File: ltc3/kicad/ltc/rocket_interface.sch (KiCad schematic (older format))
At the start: 68 parts, among them IC601 TLP3542, J601 RJ45, K601 RELAY_1C, K602 RELAY_1C, M601 W28-XQ1A-10, P601 BATT-IN, P602 CONN_01x02, P603 UMBILICAL, P604 43025-0200, P605 43045-0200, P606 S4B-PH-K, P607 43045-0200, P608 43025-0200, P609 PHR-4, Q601 PMV45EN, Q602 PMV45EN, Q603 ZVN4525E6, Q604 ZVN4525E6, Q605 ZVN4525E6, SW601 SPST, U601 CD74HC14, U602 SN65220DBV, U603 741G08

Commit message: LTC3: Split single-board design into two boards.
Separated the charge controller and cell protection circuitry onto its
own board (kicad/charge_controller).  The DC-DC converters,
BeagleBone, external power and triggers, and ignition fire control
circuitry remains together (kicad/ltc).

Both boards have had their schematics updated.  Sub-sheets for
circuitry moved to the other board were removed.  Still more work
remaining, though (e.g., add I2C connectors to Charge Controller
schematic; add battery power connector to LTC board; etc.).

Schematic components were *not* re-annotated to align with new sheet
numbering, as it would screw up the existing layout work (i.e., placed
components would disappear), and that would make us sad engineers.

Both boards have had their PCB layouts converted to four-layer.
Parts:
- D606, D608, D610, JP601, M601, P602, P604, P609, SW601: footprint OFF-BOARD -> (none)

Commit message: LTC3: Main Board Layout con't
For the most part finished a layout of the main LTC3 board!  Hooray!
Had to adjust a symbol and hoping that it doesn't mess up the library.

Todo: Figure out of this is 4 layer or 2 layer board.  May be doable as 2.
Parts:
- K601, K602: symbol RELAY_1C -> RELAY_1C-RESCUE-LTC3
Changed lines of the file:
@@
 LIBS:atmel
 LIBS:audio
+LIBS:bbd
 LIBS:brooktre
 LIBS:cmos4000
@@
 LIBS:transistors
 LIBS:ttl_ieee
+LIBS:LTC3-cache
 EELAYER 25 0
 EELAYER END
 $Descr B 17000 11000
 encoding utf-8
-Sheet 6 6
+Sheet 4 6
 Title "LTC3 Rocket Umbilical & Ignition Control"
 Date "2016-05-09"
@@
 VCC for \nCD74HC14
 $Comp
-L RELAY_1C K601
+L RELAY_1C-RESCUE-LTC3 K601
 U 1 1 5658C6AE
 P 13350 1550
+AR Path="/5658C6AE" Ref="K601"  Part="1"
+AR Path="/5598112B/5658C6AE" Ref="K601"  Part="1"
 F 0 "K601" H 13350 1890 50  0000 C CNN
 F 1 "RELAY_1C" H 13350 1200 50  0000 C CNN
@@
 $EndComp
 $Comp
-L RELAY_1C K602
+L RELAY_1C-RESCUE-LTC3 K602
 U 1 1 56704258
 P 12350 5900
+AR Path="/56704258" Ref="K602"  Part="1"
+AR Path="/5598112B/56704258" Ref="K602"  Part="1"
 F 0 "K602" H 12350 6240 50  0000 C CNN
 F 1 "RELAY_1C" H 12350 5550 50  0000 C CNN

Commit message: LTC3: Updates to LTC schematic.
1. Cleaned up top-level sheet.
2. Added board-to-board connectors for power, I2C.
3. Miscelleneous component part selection/changes.
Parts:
- removed IC601: TLP3542, Housings_DIP:DIP-6_W7.62mm, symbol TLP3542
- removed P601: BATT-IN, Connectors_Molex:Molex_Microfit3_Header_02x01_Straight_43045-0228, symbol CONN_01X02
- removed Q601: PMV45EN, TO_SOT_Packages_SMD:SOT-23, symbol PMV45EN
- added P401: MicroFit header, Connectors_Molex:Molex_Microfit3_Header_02x01_Straight_43045-0228, symbol CONN_01X02
- added Q401: PMV45EN, TO_SOT_Packages_SMD:SOT-23, symbol PMV45EN
- added U404: TLP3542, Housings_DIP:DIP-6_W7.62mm, symbol TLP3542
- C401: renamed from C601; footprint Capacitors_SMD:C_1206 -> ~; Mfg_Name (none) -> -; Mfg_PN (none) -> -; Note (none) -> -; Spec (none) -> 10V
- C402: renamed from C602; Mfg_Name (none) -> -; Mfg_PN (none) -> -; Note (none) -> -; Spec (none) -> 10V
- C403: renamed from C603; Mfg_Name (none) -> -; Mfg_PN (none) -> -; Note (none) -> -; Spec (none) -> 50V
- D401: renamed from D601; footprint Resistors_SMD:R_0603 -> Diodes_SMD:SOD-523; Mfg_Name (none) -> Comchip; Mfg_PN (none) -> CDSU4148; Note (none) -> -; Spec (none) -> -
- K401: renamed from K601; symbol RELAY_1C-RESCUE-LTC3 -> RELAY_1C
- K402: renamed from K602; symbol RELAY_1C-RESCUE-LTC3 -> RELAY_1C
- P404: renamed from P603; value UMBILICAL -> Molex Micro-Fit header; Mfg_Name (none) -> Molex; Mfg_PN (none) -> -; Spec (none) -> -
- U401: renamed from U601; Mfg_Name (none) -> TI; Mfg_PN (none) -> CD74HC14PWR; Note (none) -> -; Spec (none) -> -
- U403: renamed from U603; value 741G08 -> 74V1G08; footprint TO_SOT_Packages_SMD:SOT-353 -> LTC3:SOT323-5L; Mfg_Name (none) -> ST; Mfg_PN (none) -> 74V1G08CTR; Note (none) -> -; Spec (none) -> -
- renumbered C604 to C404, C605 to C405, C606 to C406, D602 to D402, D603 to D403, D604 to D404, D605 to D405, D609 to D406, D606 to D407, D608 to D408, D610 to D409, J601 to J401, JP601 to JP401, M601 to M401, P604 to P402, P605 to P403, P606 to P405, P607 to P406, P608 to P407, P602 to P408, P609 to P409, Q603 to Q402, Q604 to Q403, Q605 to Q404, Q602 to Q405, R603 to R401, R601 to R402, R604 to R403, R602 to R404, R605 to R405, R606 to R406, R607 to R407, R609 to R408, R608 to R409, R612 to R410, R611 to R411, R610 to R412, R613 to R413, R615 to R414, R614 to R415, R617 to R416, R618 to R417, R619 to R418, R616 to R419, R620 to R420, R622 to R421, R621 to R422, SW601 to SW401, U602 to U402, W601 to W401, W602 to W402, W603 to W403, W604 to W404, W605 to W405, W606 to W406, W607 to W407
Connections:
- net GND: now also Q401.2 (S), U404.2, U404.4
- net GND_IGN: now also P401.2 (P2)
- net IGN_BATT_P: now also P401.1 (P1)
- net at R405.1, U403.1 (A), W404.1: now also U401.1, U401.4; no longer U401.2, U401.3
- net at C401.1, C402.1, R406.1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: now also U401.5; no longer U401.9
- net at R409.1: now also U401.8, Q401.1 (G); no longer U401.6
- net at D401.2 (A), K401.5 (COIL2): now also Q401.3 (D)
- net at R402.2: now also U401.3, U404.6; no longer U401.1
- net at R404.1: now also U404.1
- net at R401.2: now also U401.2; no longer U401.4
- new net: U401.11, U401.6, U401.9
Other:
- note added: "Circuit keeps ignition battery pack disconnected until\nflight computer has asserted ROCKET_READY and\n19 VDC rail (shore power) has been shut off."
- note added: "TODO: datasheet"
- note removed: "Ignition battery pack disconnected until\nflight computer has asserted ROCKET_READY\nand 19 VDC rail (shore power) has been shut off."
- note removed: "TODO: select conn."

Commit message: LTC3: More BOM work, mostly on the LTC proper.
Plus a few minor tweaks to the charge controller and cell protection
BOMs that should not impact PCB layout.

Nearly finished with LTC BOM.
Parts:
- C401: footprint ~ -> Capacitors_SMD:C_0805; Mfg_Description (none) -> 10V X7R 10%; Mfg_Name - -> Murata; Mfg_PN - -> GRM21BR71A106KE51L
- C402, P401, Q401, U404: Mfg_Description (none) -> -
- C403: Mfg_Description (none) -> 100V X7R 10%; Mfg_Name - -> Murata; Mfg_PN - -> GCM21BR72A104KA37L
- C404: Mfg_Description (none) -> 100V X7S 10%; Mfg_Name (none) -> TDK; Mfg_PN (none) -> CGA4J3X7S2A105K125AB; Note (none) -> -; Spec (none) -> -
- C405, C406: Mfg_Description (none) -> 100V X7R 10%; Mfg_Name (none) -> Murata; Mfg_PN (none) -> GCM21BR72A104KA37L; Note (none) -> -; Spec (none) -> -
- D401: Mfg_Description (none) -> Standard 75V 150mA
- D402, D404: footprint Resistors_SMD:R_0603 -> Diodes_SMD:SOD-523; Mfg_Description (none) -> Standard 75V 150mA; Mfg_Name (none) -> Comchip; Mfg_PN (none) -> CDSU4148; Note (none) -> -; Spec (none) -> -
- D403, D405: value LED -> RED; footprint Choke_Axial_ThroughHole:Choke_Horizontal_RM10mm -> LEDs:LED_1206; Mfg_Name (none) -> Lite-On; Mfg_PN (none) -> LTST-C150CKT; Spec (none) -> -
- D406: footprint Diodes_SMD:SMA_Standard -> Diodes_SMD:SOD-323; Mfg_Description (none) -> Zener 3.3V 300mW ±6%; Mfg_Name (none) -> ON; Mfg_PN (none) -> MM3Z3V3T1G; Note (none) -> -; Spec (none) -> -
- D407: value 557-1702-203F -> Yellow, Lg.; footprint (none) -> ~; Mfg_Description (none) -> Yellow 5V 80mA 17.8mm; Mfg_Name (none) -> Dialight; Mfg_PN (none) -> 557-1702-203F; Note Batt. Relay Closed -> OFF-BOARD, Batt. Relay Closed; Spec (none) -> -
- D408: value 557-1702-203F -> Yellow, Lg.; footprint (none) -> ~; Mfg_Description (none) -> Yellow 5V 80mA 17.8mm; Mfg_Name (none) -> Dialight; Mfg_PN (none) -> 557-1702-203F; Note Ign. Relay Closed -> OFF-BOARD, Ign. Relay Closed; Spec (none) -> -
- D409: value 557-1502-203F -> Red, Lg.; footprint (none) -> ~; Mfg_Description (none) -> Red 5V 80mA 17.8mm; Mfg_Name (none) -> Dialight; Mfg_PN (none) -> 557-1502-203F; Note Ignition HOT -> OFF-BOARD, Ignition HOT; Spec (none) -> -
- J401, P405, R408: Mfg_Description (none) -> -; Mfg_Name (none) -> -; Mfg_PN (none) -> -; Note (none) -> -; Spec (none) -> -
- JP401, P402, P408: footprint (none) -> ~; Mfg_Description (none) -> -; Mfg_Name (none) -> -; Mfg_PN (none) -> -; Spec (none) -> -
- K401, K402: footprint LTC3:G5LE-14 -> ~; Mfg_Description (none) -> SPDT (1 Form C) 5VDC Coil; Mfg_Name (none) -> Omron; Mfg_PN (none) -> G5LE-14 DC5; Note (none) -> -; Spec (none) -> -
- M401: footprint (none) -> ~; Mfg_Description (none) -> 10A 250VAC 32VDC; Mfg_Name (none) -> TE; Mfg_PN (none) -> W28-XQ1A-10; Note (none) -> OFF-BOARD; Spec (none) -> -
- P403, P406, P407: Mfg_Description (none) -> -; Mfg_Name (none) -> -; Mfg_PN (none) -> -; Spec (none) -> -
- P404: Mfg_Description (none) -> -; Note (none) -> -
- P409: footprint (none) -> ~; Mfg_Description (none) -> -; Mfg_Name (none) -> -; Mfg_PN (none) -> -; Note (none) -> -; Spec (none) -> -
- Q402, Q403, Q404: Mfg_Description (none) -> MOSFET N-CH 250V 230MA; Mfg_Name (none) -> Diodes, Inc.; Mfg_PN (none) -> ZVN4525E6TA; Note (none) -> -; Spec (none) -> -
- Q405: Mfg_Description (none) -> MOSFET N-CH 30V; Mfg_Name (none) -> NXP; Mfg_PN (none) -> PMV45EN2R; Note (none) -> -; Spec (none) -> -
- R401, R411: Mfg_Description (none) -> 1% 1/8W; Mfg_Name (none) -> Yageo; Mfg_PN (none) -> RC0805FR-0762KL; Note (none) -> -; Spec (none) -> -
- R402, R405, R409, R414, R421: Mfg_Description (none) -> 1% 1/8W; Mfg_Name (none) -> Yageo; Mfg_PN (none) -> RC0805FR-0710KL; Note (none) -> -; Spec (none) -> -
- R403, R415: Mfg_Description (none) -> 1% 1/8W; Mfg_Name (none) -> Yageo; Mfg_PN (none) -> RC0805FR-07100KL; Note (none) -> -; Spec (none) -> -
- R404: Mfg_Description (none) -> 1% 1/8W; Mfg_Name (none) -> Yageo; Mfg_PN (none) -> RC0805FR-07120RL; Note (none) -> -; Spec (none) -> -
- R406: Mfg_Description (none) -> 1% 1/8W; Mfg_Name (none) -> Yageo; Mfg_PN (none) -> RC0805FR-07100RL; Note (none) -> -; Spec (none) -> -
- R407: Mfg_Description (none) -> 1% 1/8W; Mfg_Name (none) -> Yageo; Mfg_PN (none) -> RC0805FR-07510KL; Note (none) -> -; Spec (none) -> -
- R410: Mfg_Description (none) -> 1% 1/8W; Mfg_Name (none) -> Yageo; Mfg_PN (none) -> RC0805FR-075K6L; Note (none) -> -; Spec (none) -> -
- R412, R420: value 250 -> 240; Mfg_Description (none) -> 1% 1/8W; Mfg_Name (none) -> Yageo; Mfg_PN (none) -> RC0805FR-07240RL; Note (none) -> -; Spec (none) -> -
- R413: Mfg_Description (none) -> 1% 1/8W; Mfg_Name (none) -> Yageo; Mfg_PN (none) -> RC0805FR-071K5L; Note (none) -> -; Spec (none) -> -
- R416, R417, R418: Mfg_Description (none) -> 1% 1/8W; Mfg_Name (none) -> Yageo; Mfg_PN (none) -> RC0805FR-0730KL; Note (none) -> -; Spec (none) -> -
- R419, R422: Mfg_Description (none) -> 1% 1/8W; Mfg_Name (none) -> Yageo; Mfg_PN (none) -> RC0805FR-075K1L; Note (none) -> -; Spec (none) -> -
- SW401: footprint (none) -> ~; Mfg_Description (none) -> -; Mfg_Name (none) -> -; Mfg_PN (none) -> -; Note (none) -> OFF-BOARD; Spec (none) -> -
- U401: Mfg_Description (none) -> Inverter IC 6 Channel Schmitt; Mfg_Name TI -> Texas Instruments
- U402: Mfg_Description (none) -> TVS; Mfg_Name (none) -> Texas Instruments; Mfg_PN (none) -> SN65220DBVR; Note (none) -> -; Spec (none) -> -
- U403: Mfg_Description (none) -> -; Mfg_Name ST -> STMicro; Note - -> OBSOLETE PART!
- W401: value 14.8-16.8V -> TEST; Mfg_Description (none) -> -; Mfg_Name (none) -> -; Mfg_PN (none) -> -; Note (none) -> -; Spec (none) -> 14.8-16.8V
- W402, W403, W404, W405, W406: value 0/5V -> TEST; Mfg_Description (none) -> -; Mfg_Name (none) -> -; Mfg_PN (none) -> -; Note (none) -> -; Spec (none) -> 0/5V
- W407: value 0/3.3V -> TEST; Mfg_Description (none) -> -; Mfg_Name (none) -> -; Mfg_PN (none) -> -; Note (none) -> -; Spec (none) -> 0/3.3V
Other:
- note added: "TODO: add MicroFit housing\ncontacts to BOM"
- note removed: "TODO: datasheet"

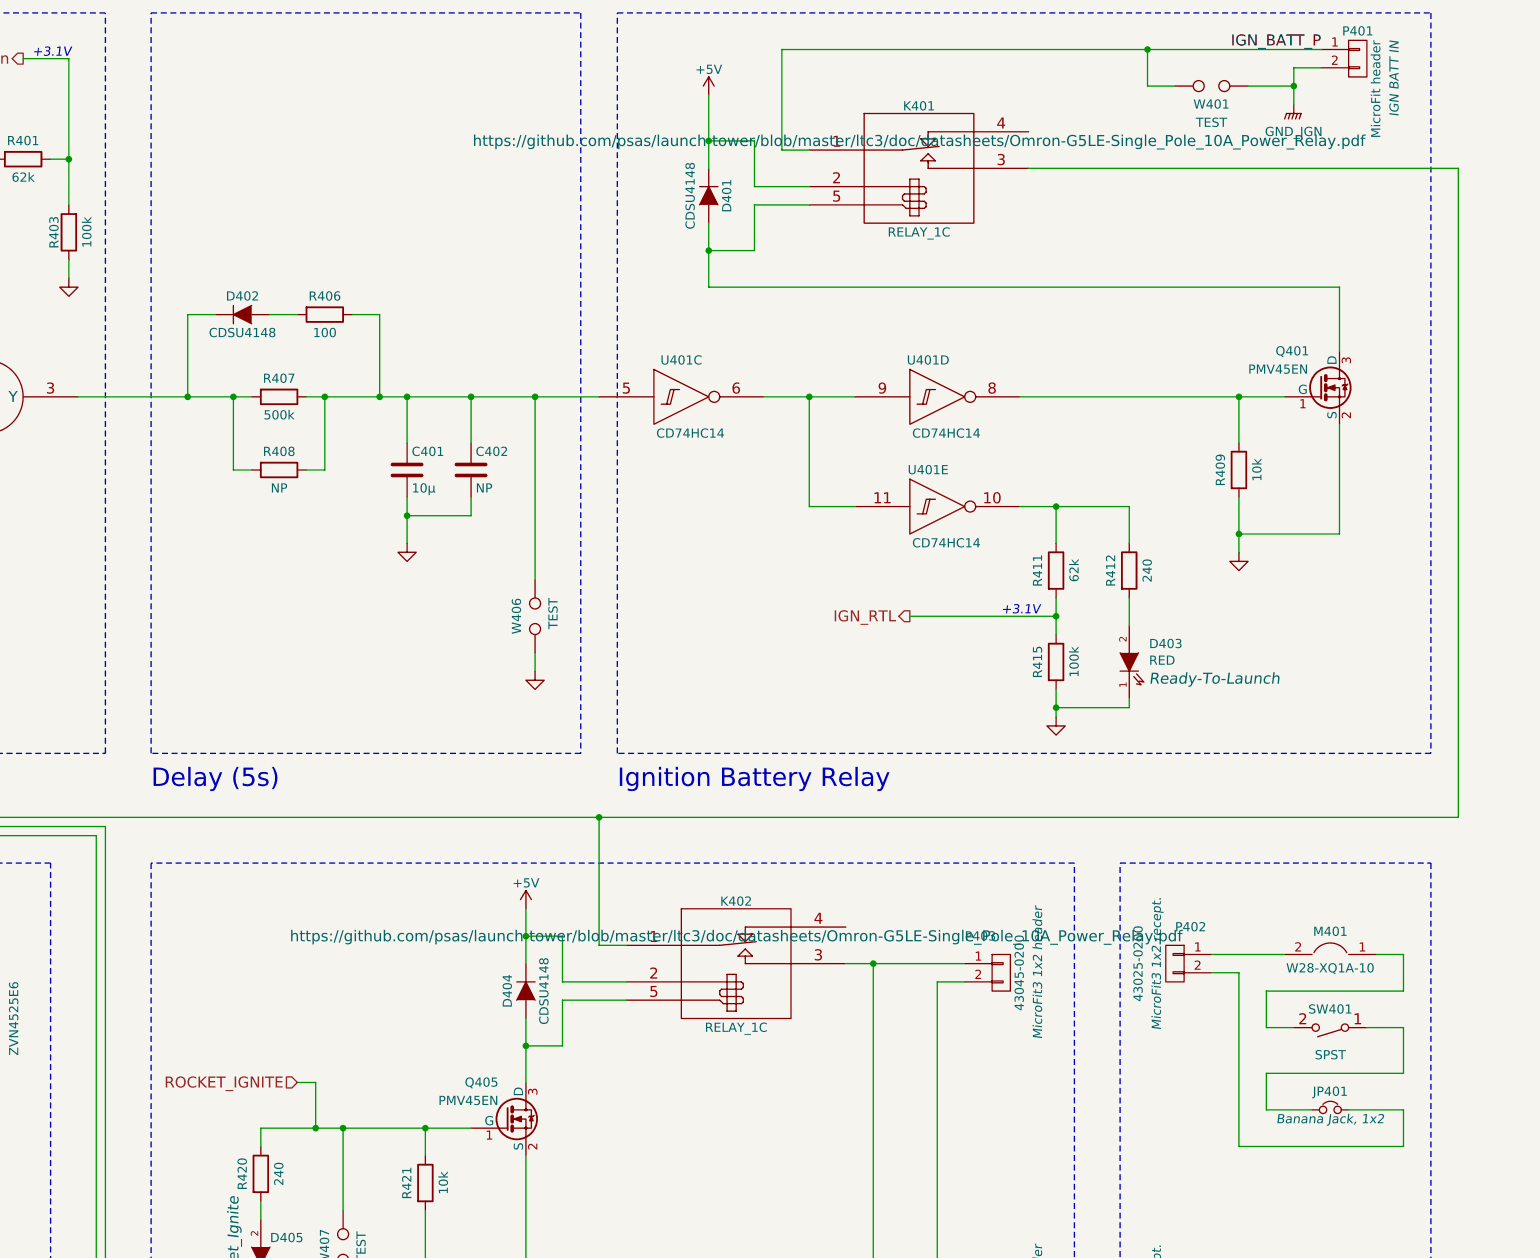
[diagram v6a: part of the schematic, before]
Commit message: LTC3: LTC schematic changes; LTC BOM work.
* Replaced LTC external power and trigger circuits' off-board manual
  override switches with board-mounted tactile momentary switches.
  Simplifies assembly, and should be more than adequate for debugging
  purposes.

* Changed cell protection diodes D1 and D6 from Rohm 1SS355 to ComChip
  CDSU4148.  CDSU4148 is already used on the LTC board, and is higher
  spec than the 1SS355.
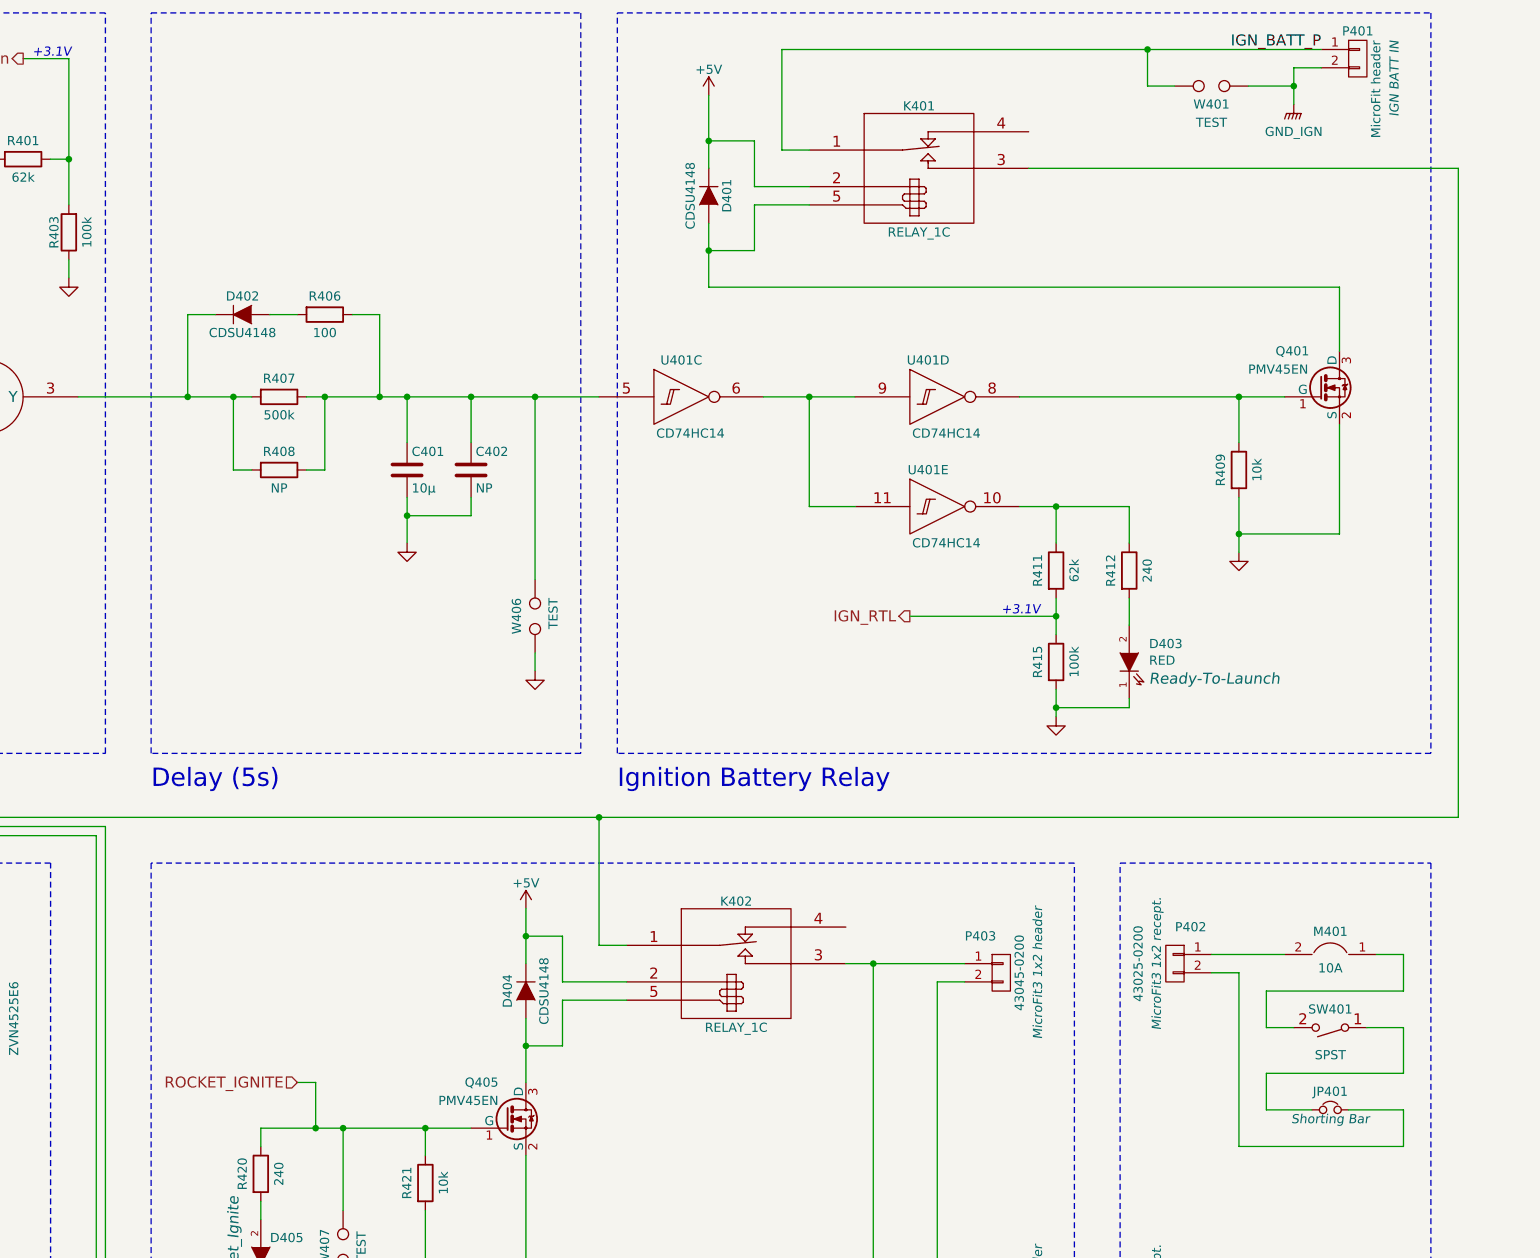
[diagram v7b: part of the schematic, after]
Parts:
- D406: Mfg_Name ON -> ON Semi
- J401: footprint Connect:RJ45_8 -> ~; Mfg_Description - -> Right angle, Shielded Cat5e; Mfg_Name - -> Stewart; Mfg_PN - -> SS-7188S-A-NF
- JP401: value Shorting Bar -> Banana Jack 1x2; Note Banana Jack, 1x2 -> Shorting Bar
- M401: value W28-XQ1A-10 -> 10A
- Q401: Mfg_Description - -> MOSFET N-CH 30V
